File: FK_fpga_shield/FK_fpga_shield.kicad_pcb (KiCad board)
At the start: 4 copper layers, 182.2 x 125 mm, 136 parts, among them J0 USB_B_Mini, J1 molex-51382-0400-microclasp, J10 molex-51382-0400-microclasp, J11 molex-51382-0400-microclasp, J12 molex-51382-0400-microclasp, J13 molex-51382-0400-microclasp, J14 molex-51382-0400-microclasp, J15 molex-51382-0400-microclasp, J16 molex-51382-0400-microclasp, J17 molex-51382-0400-microclasp, J18 molex-51382-0400-microclasp, J19 molex-51382-0400-microclasp, J2 molex-51382-0400-microclasp, J20 molex-51382-0400-microclasp, J21 molex-51382-0400-microclasp, J22 molex-51382-0400-microclasp, J23 molex-51382-0400-microclasp, J24 molex-51382-0400-microclasp, J25 molex-51382-0400-microclasp, J26 molex-51382-0400-microclasp, J27 molex-51382-0400-microclasp, J28 molex-51382-0400-microclasp, J29 molex-51382-0400-microclasp, J3 molex-51382-0400-microclasp, J30 molex-51382-0400-microclasp, J31 molex-51382-0400-microclasp, J32 molex-51382-0400-microclasp, J33 molex-51382-0400-microclasp, J34 molex-51382-0400-microclasp, J35 molex-51382-0400-microclasp, J4 molex-51382-0400-microclasp, J5 molex-51382-0400-microclasp, J6 molex-51382-0400-microclasp, J7 molex-51382-0400-microclasp, J8 molex-51382-0400-microclasp, J9 molex-51382-0400-microclasp, U1 FT232RL, U2 nvt2010pw, U3 nvt2010pw, U4 nvt2010pw, U5 nvt2010pw, U6 nvt2010pw, U7 nvt2010pw, U8 nvt2010pw

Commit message: fix u6
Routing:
- net Net-(J22-Pad4): track 0.00 -> 31.4 mm
- net Net-(J22-Pad2): track 0.00 -> 31.0 mm
- net Net-(J21-Pad2): track 0.00 -> 30.7 mm
- net Net-(J23-Pad4): track 0.00 -> 30.1 mm
- net Net-(J21-Pad4): track 0.00 -> 29.2 mm
- net Net-(J23-Pad2): track 0.00 -> 26.0 mm
- net Net-(J24-Pad4): track 0.00 -> 22.1 mm
- net Net-(J24-Pad2): track 0.00 -> 21.5 mm
- net Net-(J25-Pad4): track 0.00 -> 21.2 mm
- net Net-(J25-Pad2): track 0.00 -> 20.2 mm
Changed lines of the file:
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@@
     (thickness 1.6)
     (drawings 17)
-    (tracks 708)
+    (tracks 753)
     (zones 0)
     (modules 136)
@@
   (segment (start 228.75 94.680666) (end 224.255666 99.175) (width 0.4) (layer F.Cu) (net 44))
   (segment (start 228.75 89.5) (end 228.75 94.680666) (width 0.4) (layer F.Cu) (net 44))
+  (segment (start 217.8625 128.375) (end 219.425 128.375) (width 0.4) (layer F.Cu) (net 45))
+  (segment (start 219.425 128.375) (end 221 126.8) (width 0.4) (layer F.Cu) (net 45))
+  (segment (start 230.375 126.8) (end 242.8 139.225) (width 0.4) (layer F.Cu) (net 45))
+  (segment (start 221 126.8) (end 230.375 126.8) (width 0.4) (layer F.Cu) (net 45))
   (segment (start 210.625 53) (end 210.625 59.375) (width 0.4) (layer F.Cu) (net 46))
   (segment (start 218.75001 69.632114) (end 218.407124 69.975) (width 0.4) (layer F.Cu) (net 46))
@@
   (segment (start 226.5 87.275) (end 242.8 70.975) (width 0.4) (layer F.Cu) (net 47))
   (segment (start 226.5 96.082124) (end 226.5 87.275) (width 0.4) (layer F.Cu) (net 47))
+  (segment (start 218.657124 127.725) (end 219.6 126.782124) (width 0.4) (layer F.Cu) (net 48))
+  (segment (start 217.8625 127.725) (end 218.657124 127.725) (width 0.4) (layer F.Cu) (net 48))
+  (segment (start 219.6 126.782124) (end 219.617876 126.782124) (width 0.4) (layer F.Cu) (net 48))
+  (segment (start 219.617876 126.782124) (end 221 125.4) (width 0.4) (layer F.Cu) (net 48))
+  (segment (start 234.825 125.4) (end 242.8 133.375) (width 0.4) (layer F.Cu) (net 48))
+  (segment (start 221 125.4) (end 234.825 125.4) (width 0.4) (layer F.Cu) (net 48))
   (segment (start 168.225 61.3375) (end 168.225 59.94725) (width 0.4) (layer F.Cu) (net 49))
   (segment (start 168.225 59.94725) (end 161.27775 53) (width 0.4) (layer F.Cu) (net 49))
@@
   (segment (start 224.873542 100.475) (end 223.2625 100.475) (width 0.4) (layer F.Cu) (net 51))
   (segment (start 231.25 97) (end 228.348542 97) (width 0.4) (layer F.Cu) (net 51))
+  (segment (start 217.8625 129.675) (end 227.075 129.675) (width 0.4) (layer F.Cu) (net 52))
+  (segment (start 238.85849 141.45849) (end 238.85849 146.63146) (width 0.4) (layer F.Cu) (net 52))
+  (segment (start 227.075 129.675) (end 238.85849 141.45849) (width 0.4) (layer F.Cu) (net 52))
   (segment (start 163.629208 56.2) (end 157.825 56.2) (width 0.4) (layer F.Cu) (net 53))
   (segment (start 157.825 56.2) (end 154.625 53) (width 0.4) (layer F.Cu) (net 53))
@@
   (segment (start 242.8 84.775) (end 239.725 84.775) (width 0.4) (layer F.Cu) (net 55))
   (segment (start 239.725 84.775) (end 224.72499 99.77501) (width 0.4) (layer F.Cu) (net 55))
+  (segment (start 217.8625 129.025) (end 220.575 129.025) (width 0.4) (layer F.Cu) (net 56))
+  (segment (start 220.575 129.025) (end 221.4 128.2) (width 0.4) (layer F.Cu) (net 56))
+  (segment (start 228.700178 128.2) (end 242.995064 142.494886) (width 0.4) (layer F.Cu) (net 56))
+  (segment (start 221.4 128.2) (end 228.700178 128.2) (width 0.4) (layer F.Cu) (net 56))
   (segment (start 169.525 61.3375) (end 169.525 61.025) (width 0.4) (layer F.Cu) (net 57))
   (segment (start 169.525 61.025) (end 169.57499 60.97501) (width 0.4) (layer F.Cu) (net 57))
@@
   (segment (start 241.75 101.775) (end 242.8 102.825) (width 0.4) (layer F.Cu) (net 59))
   (segment (start 223.2625 101.775) (end 241.75 101.775) (width 0.4) (layer F.Cu) (net 59))
+  (segment (start 217.8625 130.975) (end 221.375 130.975) (width 0.4) (layer F.Cu) (net 60))
+  (segment (start 231.575 141.175) (end 231.575 149.2) (width 0.4) (layer F.Cu) (net 60))
+  (segment (start 221.375 130.975) (end 231.575 141.175) (width 0.4) (layer F.Cu) (net 60))
   (segment (start 168.875 61.3375) (end 168.875 56.65) (width 0.4) (layer F.Cu) (net 61))
   (segment (start 168.875 56.65) (end 165.225 53) (width 0.4) (layer F.Cu) (net 61))
@@
   (segment (start 225.5 100.75) (end 225.447084 100.75) (width 0.4) (layer F.Cu) (net 63))
   (segment (start 227 99.25) (end 225.5 100.75) (width 0.4) (layer F.Cu) (net 63))
+  (segment (start 218.17499 130.37499) (end 223.17499 130.37499) (width 0.4) (layer F.Cu) (net 64))
+  (segment (start 217.8625 130.325) (end 218.125 130.325) (width 0.4) (layer F.Cu) (net 64))
+  (segment (start 218.125 130.325) (end 218.17499 130.37499) (width 0.4) (layer F.Cu) (net 64))
+  (segment (start 223.17499 130.37499) (end 235.8 143) (width 0.4) (layer F.Cu) (net 64))
+  (segment (start 235.8 147.575) (end 237.425 149.2) (width 0.4) (layer F.Cu) (net 64))
+  (segment (start 235.8 143) (end 235.8 147.575) (width 0.4) (layer F.Cu) (net 64))
   (segment (start 174.169334 57) (end 177.175 57) (width 0.4) (layer F.Cu) (net 65))
   (segment (start 177.175 57) (end 181.075 53.1) (width 0.4) (layer F.Cu) (net 65))
@@
   (segment (start 236.075 108.5) (end 242.8 115.225) (width 0.4) (layer F.Cu) (net 67))
   (segment (start 231.901458 108.5) (end 236.075 108.5) (width 0.4) (layer F.Cu) (net 67))
+  (segment (start 217.8625 132.275) (end 220.426458 132.275) (width 0.4) (layer F.Cu) (net 68))
+  (segment (start 220.426458 132.275) (end 222.2 134.048542) (width 0.4) (layer F.Cu) (net 68))
+  (segment (start 222.2 134.048542) (end 222.2 136.4) (width 0.4) (layer F.Cu) (net 68))
+  (segment (start 219.075 139.525) (end 219.075 149.2) (width 0.4) (layer F.Cu) (net 68))
+  (segment (start 222.2 136.4) (end 219.075 139.525) (width 0.4) (layer F.Cu) (net 68))
   (segment (start 170.175 61.3375) (end 170.175 58.15) (width 0.4) (layer F.Cu) (net 69))
   (segment (start 170.175 58.15) (end 175.225 53.1) (width 0.4) (layer F.Cu) (net 69))
@@
   (segment (start 223.2625 102.425) (end 226.675 102.425) (width 0.4) (layer F.Cu) (net 71))
   (segment (start 226.675 102.425) (end 230 105.75) (width 0.4) (layer F.Cu) (net 71))
+  (segment (start 223.6 147.875) (end 224.925 149.2) (width 0.4) (layer F.Cu) (net 72))
+  (segment (start 218.657124 131.625) (end 218.682124 131.6) (width 0.4) (layer F.Cu) (net 72))
+  (segment (start 217.8625 131.625) (end 218.657124 131.625) (width 0.4) (layer F.Cu) (net 72))
+  (segment (start 220.6 131.6) (end 223.6 134.6) (width 0.4) (layer F.Cu) (net 72))
+  (segment (start 218.682124 131.6) (end 220.6 131.6) (width 0.4) (layer F.Cu) (net 72))
+  (segment (start 223.6 134.6) (end 223.6 147.875) (width 0.4) (layer F.Cu) (net 72))
   (segment (start 194.675 53.1) (end 186.4375 61.3375) (width 0.4) (layer F.Cu) (net 73))
   (segment (start 186.4375 61.3375) (end 172.125 61.3375) (width 0.4) (layer F.Cu) (net 73))
@@
   (segment (start 223.2625 108.087499) (end 242.800001 127.625) (width 0.4) (layer F.Cu) (net 75))
   (segment (start 223.2625 104.375) (end 223.2625 108.087499) (width 0.4) (layer F.Cu) (net 75))
+  (segment (start 217.8625 133.575) (end 208.2 143.2375) (width 0.4) (layer F.Cu) (net 76))
+  (segment (start 206.875 144.5625) (end 208.2 143.2375) (width 0.4) (layer F.Cu) (net 76))
+  (segment (start 206.875 149.2) (end 206.875 144.5625) (width 0.4) (layer F.Cu) (net 76))
   (segment (start 182.625 59.2) (end 188.825 53) (width 0.4) (layer F.Cu) (net 77))
   (segment (start 171.475 61.3375) (end 171.475 60.542876) (width 0.4) (layer F.Cu) (net 77))
@@
   (segment (start 224.057124 103.725) (end 242.107124 121.775) (width 0.4) (layer F.Cu) (net 79))
   (segment (start 223.2625 103.725) (end 224.057124 103.725) (width 0.4) (layer F.Cu) (net 79))
+  (segment (start 217.8625 132.925) (end 219.125 132.925) (width 0.4) (layer F.Cu) (net 80))
+  (segment (start 219.125 132.925) (end 220.4 134.2) (width 0.4) (layer F.Cu) (net 80))
+  (segment (start 220.4 134.2) (end 220.4 135.4) (width 0.4) (layer F.Cu) (net 80))
+  (segment (start 212.725 143.075) (end 212.725 149.2) (width 0.4) (layer F.Cu) (net 80))
+  (segment (start 220.4 135.4) (end 212.725 143.075) (width 0.4) (layer F.Cu) (net 80))
   (segment (start 189.725 149.2) (end 189.725 146.975) (width 0.4) (layer F.Cu) (net 81))
   (segment (start 189.725 146.975) (end 186.75 144) (width 0.4) (layer F.Cu) (net 81))

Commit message: wip routing (usb done (?))
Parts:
- added C12: dnp, Capacitor_SMD:C_0805_2012Metric_Pad1.15x1.40mm_HandSolder, F.Cu at (108.8, 117.6)
- added C13: dnp, Capacitor_SMD:C_0805_2012Metric_Pad1.15x1.40mm_HandSolder, F.Cu at (108.8, 113.8)
- added Y1: DNP_(12MHz), Crystal:Crystal_SMD_HC49-SD, F.Cu at (105.0, 116.0)
- C4: footprint Capacitor_SMD:C_0805_2012Metric_Pad1.15x1.40mm_HandSolder -> Capacitor_THT:CP_Radial_D4.0mm_P1.50mm
- moved C4 274.6 mm to (98.6, 122.0)
- moved C2 272.5 mm to (96.0, 122.0), turned to 270 degrees
- moved R79 252.7 mm to (121.0, 141.0), turned to 180 degrees
- moved C11 213.2 mm to (117.8, 140.0), turned to 90 degrees
- moved C5 196.8 mm to (102.2, 62.2), turned to 270 degrees
- moved C9 193.6 mm to (216.8, 124.0), turned to 180 degrees
- moved R54 190.2 mm to (159.8, 61.2)
- moved C6 185.9 mm to (163.0, 62.2), turned to 270 degrees
- moved C10 176.2 mm to (174.6, 139.6), turned to 90 degrees
- moved R78 172.4 mm to (177.8, 140.6), turned to 180 degrees
- moved R57 134.3 mm to (217.8, 121.0), turned to 270 degrees
- moved C7 124.2 mm to (213.8, 66.6), turned to 180 degrees
- moved C8 120.9 mm to (222.4, 95.0), turned to 180 degrees
- moved C1 97.9 mm to (89.6, 121.2), turned to 180 degrees
- moved C3 97.3 mm to (94.0, 122.0), turned to 270 degrees
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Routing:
- net /5V: track 0.00 -> 283.1 mm, vias 0 -> 7
- net /3V3: track 11.3 -> 197.9 mm, vias 0 -> 4
- net GND: track 15.4 -> 90.1 mm, vias 1 -> 11
- net /RX: track 0.00 -> 69.8 mm
- net /TX: track 0.00 -> 59.8 mm
- net Net-(J22-Pad4): track 31.4 -> 46.8 mm
- net Net-(C1-Pad1): track 0.00 -> 14.8 mm
- net Net-(J22-Pad2): track 31.0 -> 44.8 mm
- net Net-(J14-Pad2): track 31.9 -> 44.9 mm
- net Net-(C13-Pad1): track 0.00 -> 12.2 mm
- net Net-(C12-Pad1): track 0.00 -> 12.1 mm
- net Net-(J14-Pad4): track 32.3 -> 43.7 mm
- net Net-(J35-Pad4): track 19.7 -> 29.7 mm
- net Net-(J26-Pad2): track 24.9 -> 34.7 mm
- net Net-(J9-Pad4): track 10.3 -> 19.7 mm
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- added copper zone on In2.Cu, net /5V
- added copper zone on F.Cu, net GND
- added copper zone on In1.Cu, net GND
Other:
- board size 182.2 x 125 mm -> 182 x 125 mm
- board text added: "Optional - do not populate box if using internal oscillator"

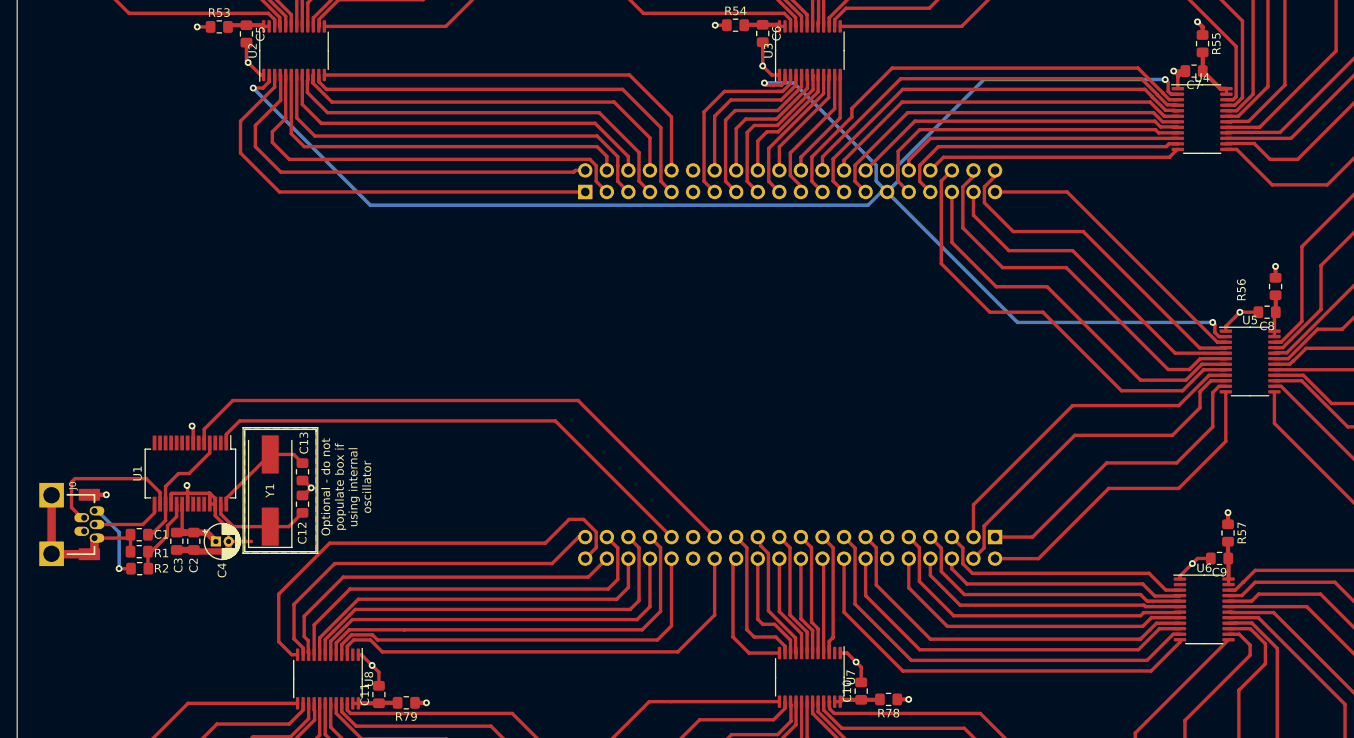
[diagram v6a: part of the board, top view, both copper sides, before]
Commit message: decouple 3V3 references just in case
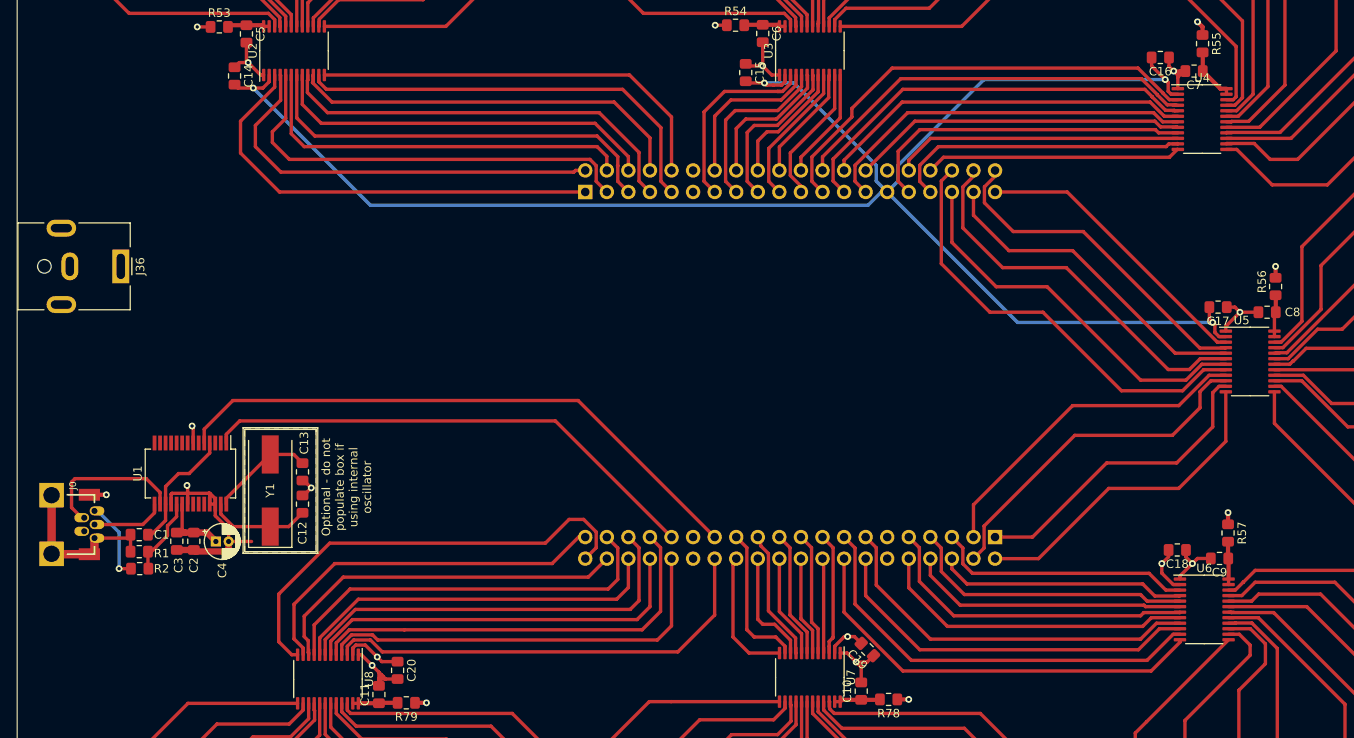
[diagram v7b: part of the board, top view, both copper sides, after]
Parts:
- added C14: 100n, Capacitor_SMD:C_0805_2012Metric_Pad1.15x1.40mm_HandSolder, F.Cu at (100.8, 67.2)
- added C15: 100n, Capacitor_SMD:C_0805_2012Metric_Pad1.15x1.40mm_HandSolder, F.Cu at (161.0, 66.8)
- added C16: 100n, Capacitor_SMD:C_0805_2012Metric_Pad1.15x1.40mm_HandSolder, F.Cu at (209.8, 65.0)
- added C17: 100n, Capacitor_SMD:C_0805_2012Metric_Pad1.15x1.40mm_HandSolder, F.Cu at (216.6, 94.4)
- added C18: 100n, Capacitor_SMD:C_0805_2012Metric_Pad1.15x1.40mm_HandSolder, F.Cu at (211.8, 123.0)
- added C19: 100n, Capacitor_SMD:C_0805_2012Metric_Pad1.15x1.40mm_HandSolder, F.Cu at (175.3, 134.7)
- added C20: 100n, Capacitor_SMD:C_0805_2012Metric_Pad1.15x1.40mm_HandSolder, F.Cu at (120.0, 137.2)
- added J36: Barrel_Jack_MountingPin, Connector_BarrelJack:BarrelJack_CUI_PJ-063AH_Horizontal, F.Cu at (87.4, 89.6)
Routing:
- net /3V3: track 197.9 -> 225.1 mm, vias 4 -> 7
- net GND: track 90.1 -> 106.2 mm

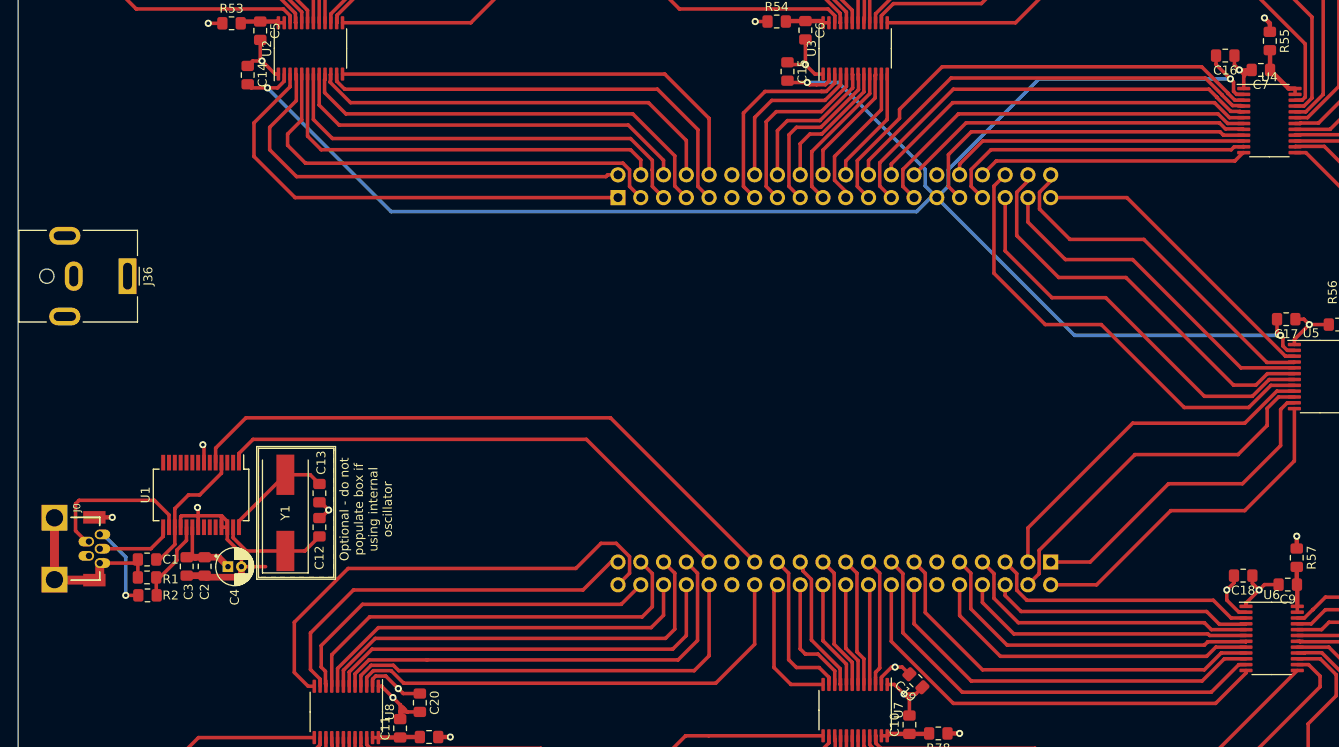
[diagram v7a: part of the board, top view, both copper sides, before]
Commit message: redo 3v3 routing
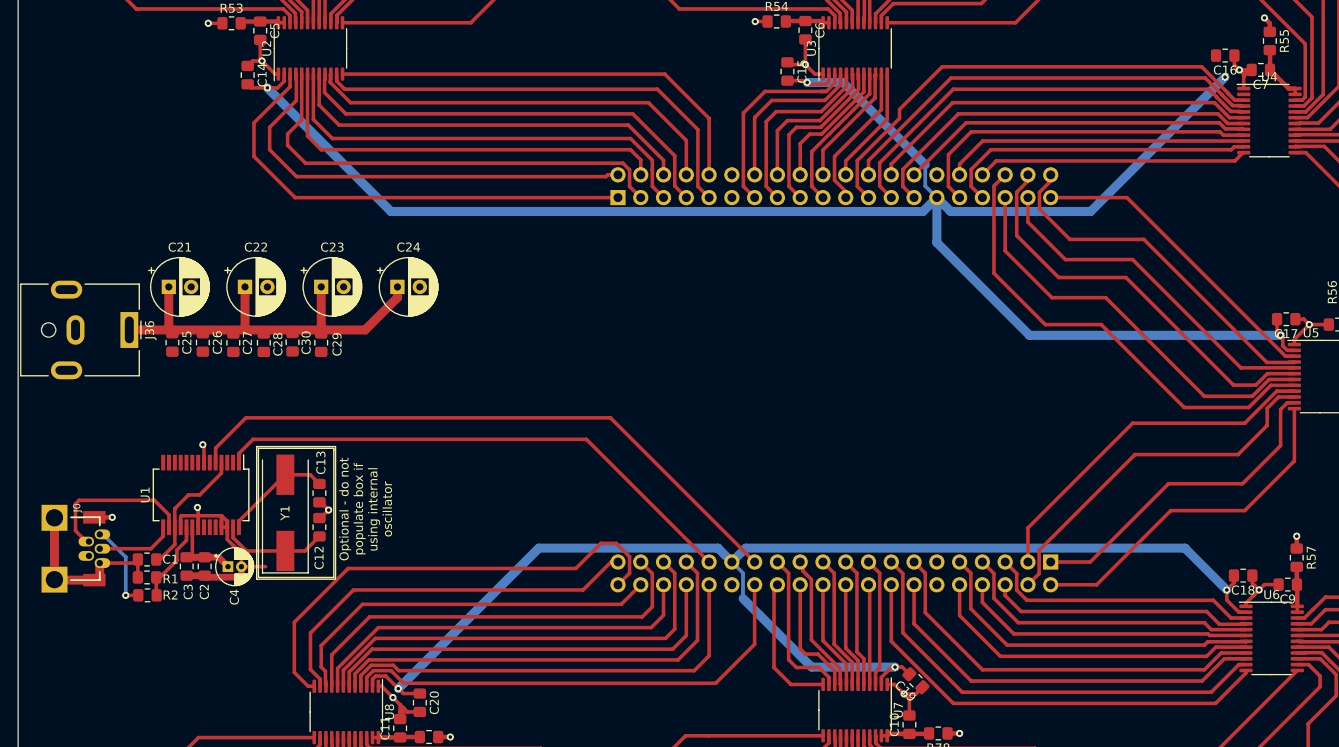
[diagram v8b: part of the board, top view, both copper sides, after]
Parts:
- added C21: 22u, Capacitor_THT:CP_Radial_D6.3mm_P2.50mm, F.Cu at (92.0, 90.8)
- added C22: 22u, Capacitor_THT:CP_Radial_D6.3mm_P2.50mm, F.Cu at (100.5, 90.8)
- added C23: 22u, Capacitor_THT:CP_Radial_D6.3mm_P2.50mm, F.Cu at (109.0, 90.8)
- added C24: 22u, Capacitor_THT:CP_Radial_D6.3mm_P2.50mm, F.Cu at (117.5, 90.8)
- added C25: 100n, Capacitor_SMD:C_0805_2012Metric_Pad1.15x1.40mm_HandSolder, F.Cu at (92.4, 97.0)
- added C26: 1u_MCC, Capacitor_SMD:C_0805_2012Metric_Pad1.15x1.40mm_HandSolder, F.Cu at (95.8, 97.0)
- added C27: DNP_10n, Capacitor_SMD:C_0805_2012Metric_Pad1.15x1.40mm_HandSolder, F.Cu at (99.2, 97.0)
- added C28: DNP_10n, Capacitor_SMD:C_0805_2012Metric_Pad1.15x1.40mm_HandSolder, F.Cu at (102.6, 97.0)
- added C29: DNP_1n, Capacitor_SMD:C_0805_2012Metric_Pad1.15x1.40mm_HandSolder, F.Cu at (105.8, 97.0)
- added C30: DNP_1n, Capacitor_SMD:C_0805_2012Metric_Pad1.15x1.40mm_HandSolder, F.Cu at (109.0, 97.0)
- moved J36 6.00 mm to (87.6, 95.6)
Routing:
- net /3V3: track 225.1 -> 349.1 mm
- net /5V: track 283.1 -> 330.1 mm
